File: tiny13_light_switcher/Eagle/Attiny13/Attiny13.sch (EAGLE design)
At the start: 39 parts, among them Q4 2N7000, Q5 2N7000, Q6 2N7000, U1 ATTiny13, U2 ATTiny85

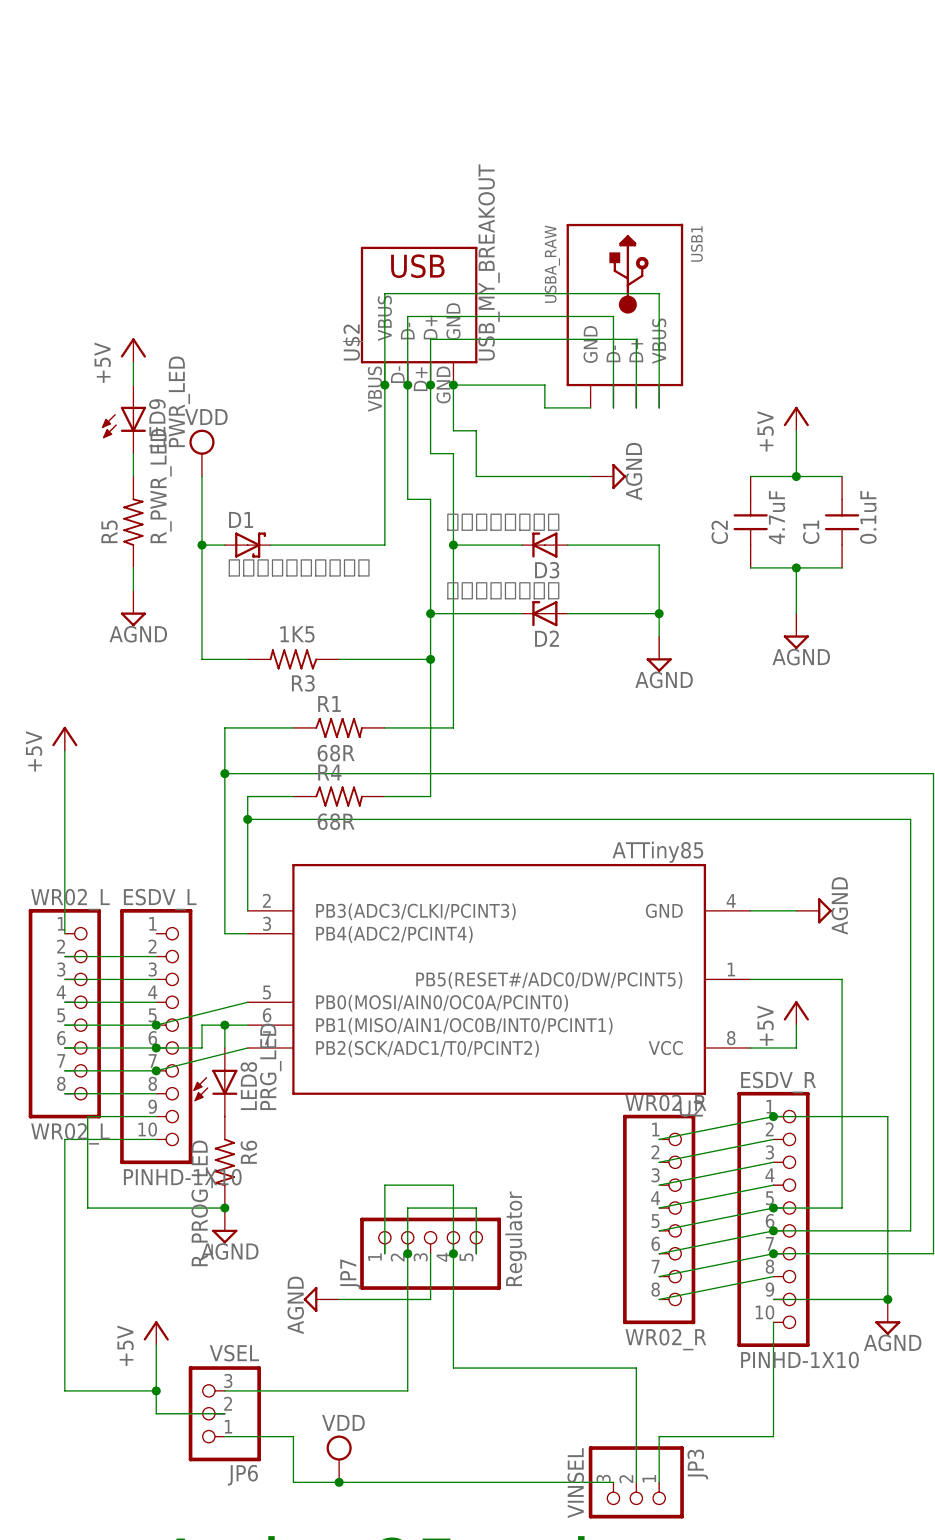
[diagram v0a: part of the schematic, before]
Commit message: Resolve DRC & ERC.
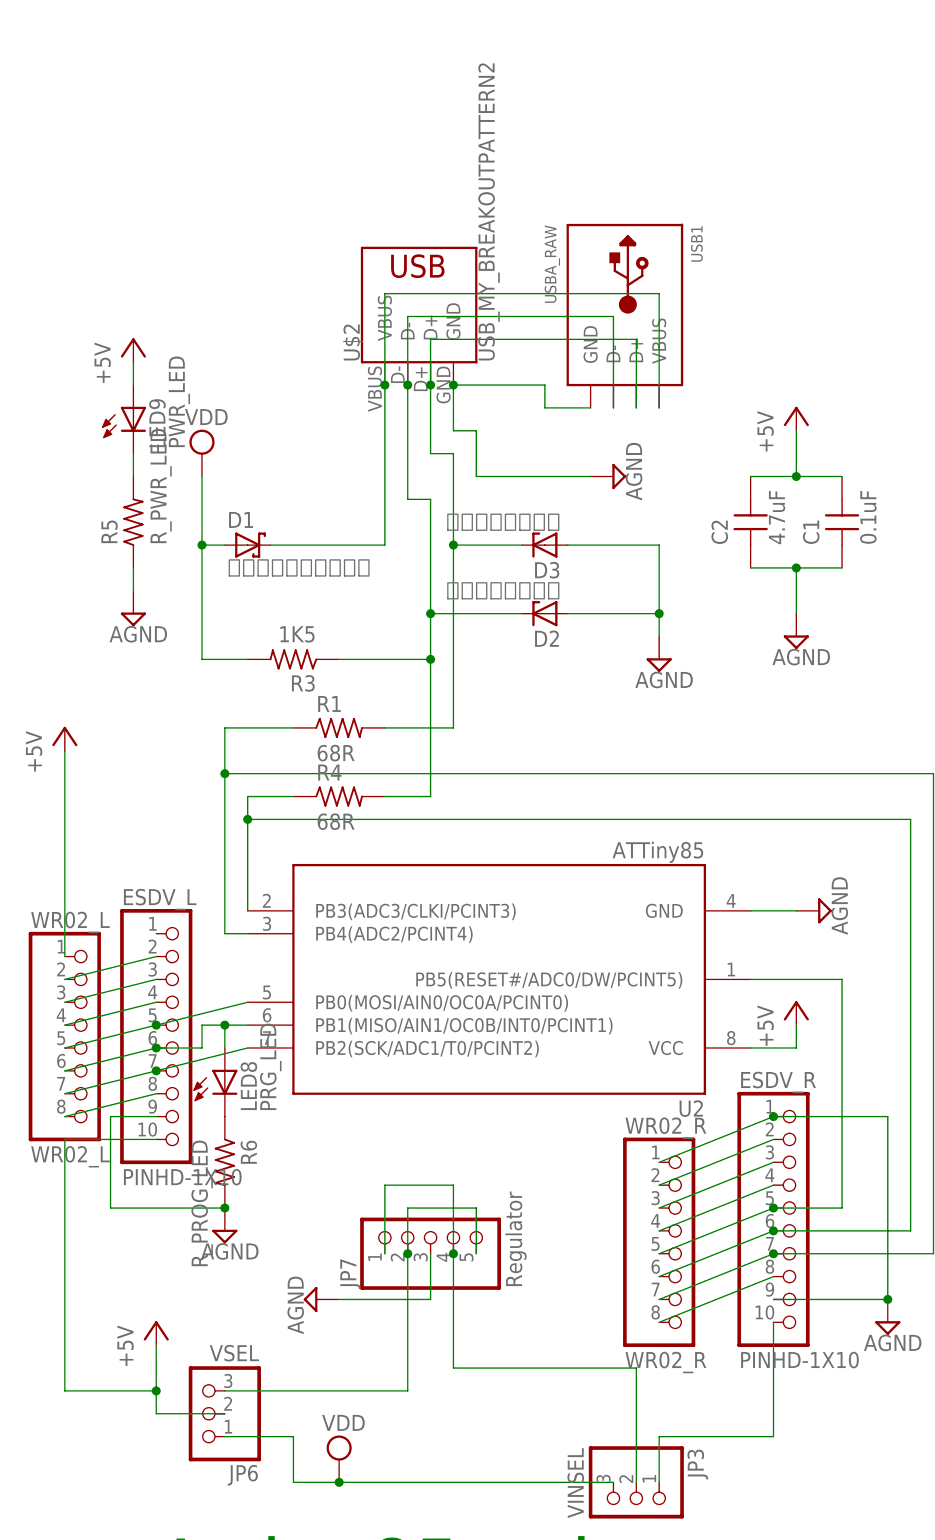
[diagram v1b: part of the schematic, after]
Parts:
- C5: device MyLib:CAPDIP_1 -> MyLib:CAPDIP_2
- U$2: value USB_MY_BREAKOUT -> USB_MY_BREAKOUTPATTERN2; device MyParts:USB_MY_BREAKOUT -> MyParts:USB_MY_BREAKOUTPATTERN2
- WR02_L, WR02_R: device pinhead:PINHD-1X8 -> adafruit:PINHD-1X8BIG
